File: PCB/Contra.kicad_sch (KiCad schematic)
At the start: 11 parts, among them J1 Conn_01x03, J2 Conn_01x02, SW1 SW_PUSH, SW2 SW_SPDT, U1 ProMicro

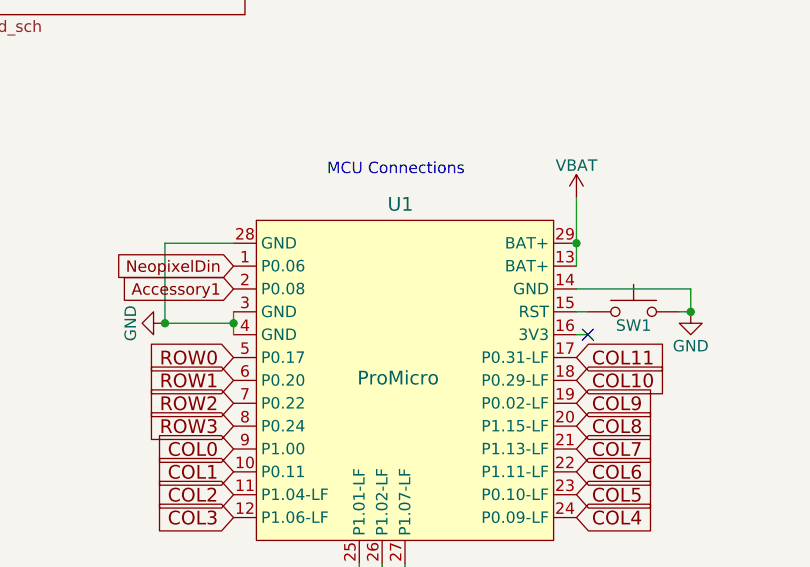
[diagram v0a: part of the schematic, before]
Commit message: reorg symbols to be locally stored
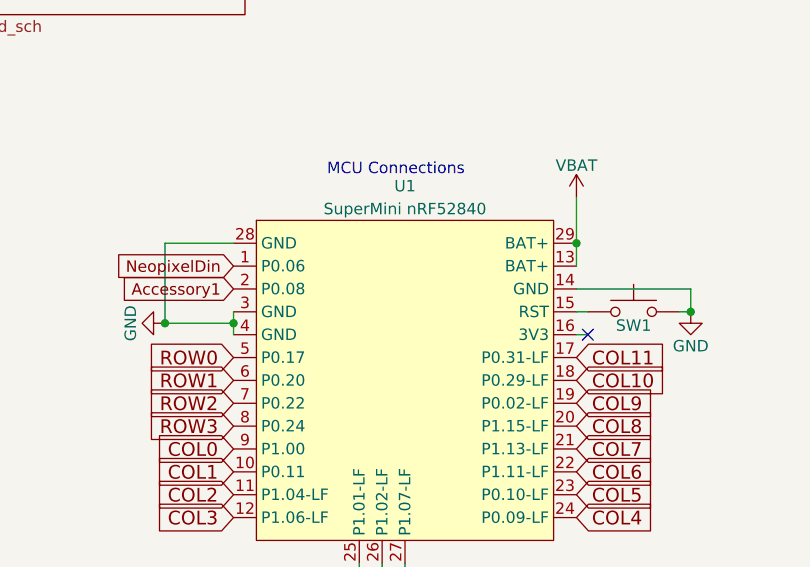
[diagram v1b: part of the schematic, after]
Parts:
- OL1: symbol kbd:OLED -> Local-lib:OLED
- U1: value ProMicro -> SuperMini nRF52840; footprint Reilly_Components:SuperMini NRF52840 -> PCM_marbastlib-xp-promicroish:SuperMini_nRF52840_AH_USBup; symbol Reilly_Components:nice_nano -> Local-lib:SuperMini_nRF52840
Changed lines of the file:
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@@
 	)
 	(symbol
-		(lib_id "Reilly_Components:nice_nano")
+		(lib_id "Local-lib:SuperMini_nRF52840")
 		(at 92.71 139.7 0)
 		(unit 1)
@@
 		(dnp no)
 		(property "Reference" "U1"
-			(at 92.202 118.872 0)
-			(show_name no)
-			(do_not_autoplace no)
-			(effects
-				(font
-					(size 1.524 1.524)
-				)
-			)
-		)
-		(property "Value" "ProMicro"
-			(at 91.948 138.176 0)
-			(show_name no)
-			(do_not_autoplace no)
-			(effects
-				(font
-					(size 1.524 1.524)
-				)
-			)
-		)
-		(property "Footprint" "Reilly_Components:SuperMini NRF52840"
+			(at 92.71 116.84 0)
+			(show_name no)
+			(do_not_autoplace no)
+			(effects
+				(font
+					(size 1.27 1.27)
+				)
+			)
+		)
+		(property "Value" "SuperMini nRF52840"
+			(at 92.71 119.38 0)
+			(show_name no)
+			(do_not_autoplace no)
+			(effects
+				(font
+					(size 1.27 1.27)
+				)
+			)
+		)
+		(property "Footprint" "PCM_marbastlib-xp-promicroish:SuperMini_nRF52840_AH_USBup"
 			(at 92.71 170.18 0)
 			(hide yes)
@@
 			)
 		)
-		(property "Datasheet" "https://nicekeyboards.com/docs/nice-nano/pinout-schematic"
+		(property "Datasheet" "https://wiki.icbbuy.com/doku.php?id=developmentboard:nrf52840"
 			(at 93.98 172.72 0)
 			(hide yes)
@@
 	)
 	(symbol
-		(lib_id "kbd:OLED")
+		(lib_id "Local-lib:OLED")
 		(at 110.49 175.26 0)
 		(unit 1)

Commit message: update to use local footprints
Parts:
- OL1: footprint kbd:OLED -> Local-lib:OLED
- U1: footprint PCM_marbastlib-xp-promicroish:SuperMini_nRF52840_AH_USBup -> Local-lib:SuperMini NRF52840
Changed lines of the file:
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@@
 			)
 		)
-		(property "Footprint" "PCM_marbastlib-xp-promicroish:SuperMini_nRF52840_AH_USBup"
+		(property "Footprint" "Local-lib:SuperMini NRF52840"
 			(at 92.71 170.18 0)
 			(hide yes)
@@
 			)
 		)
-		(property "Footprint" "kbd:OLED"
+		(property "Footprint" "Local-lib:OLED"
 			(at 110.49 172.72 0)
 			(hide yes)

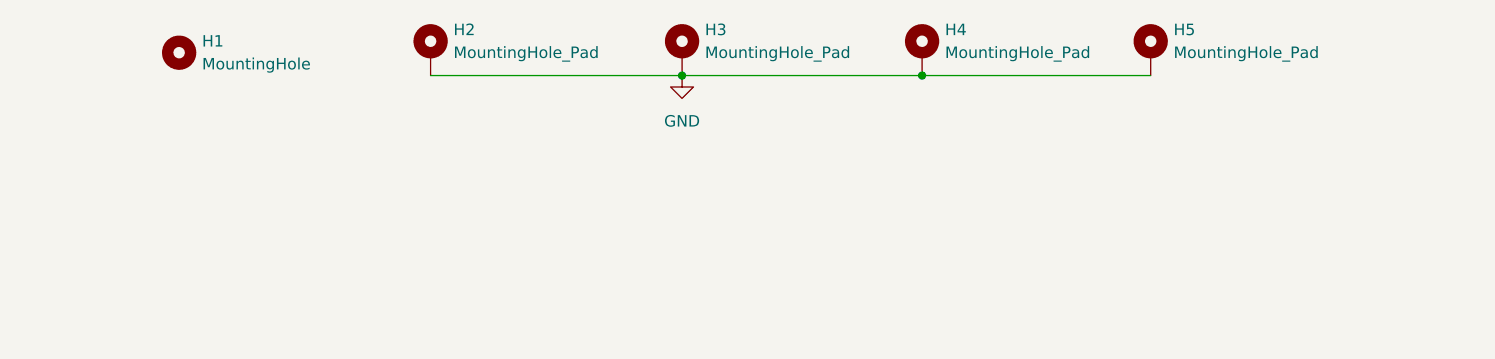
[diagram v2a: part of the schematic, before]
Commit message: update 1u footprints adjust spacing
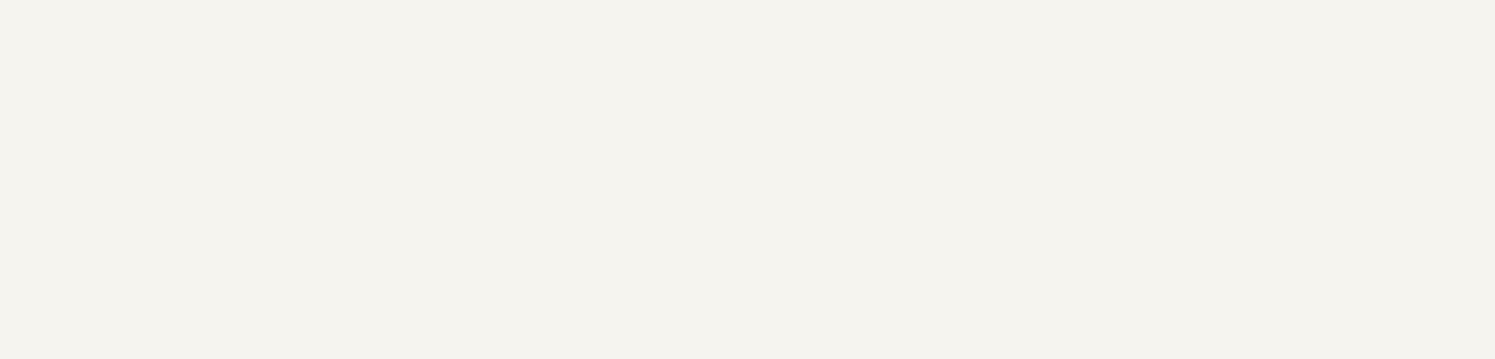
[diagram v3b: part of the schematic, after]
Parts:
- removed H1: MountingHole, MountingHole:MountingHole_2.2mm_M2, symbol Mechanical:MountingHole
- removed H2, H3, H4, H5: MountingHole_Pad, MountingHole:MountingHole_2.2mm_M2_Pad, symbol Mechanical:MountingHole_Pad
